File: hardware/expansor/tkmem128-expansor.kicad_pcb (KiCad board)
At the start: 2 copper layers, 78.7 x 45 mm, 4 parts, among them J1 Barramento TK, J2 Passagem, J3 Para a placa principal

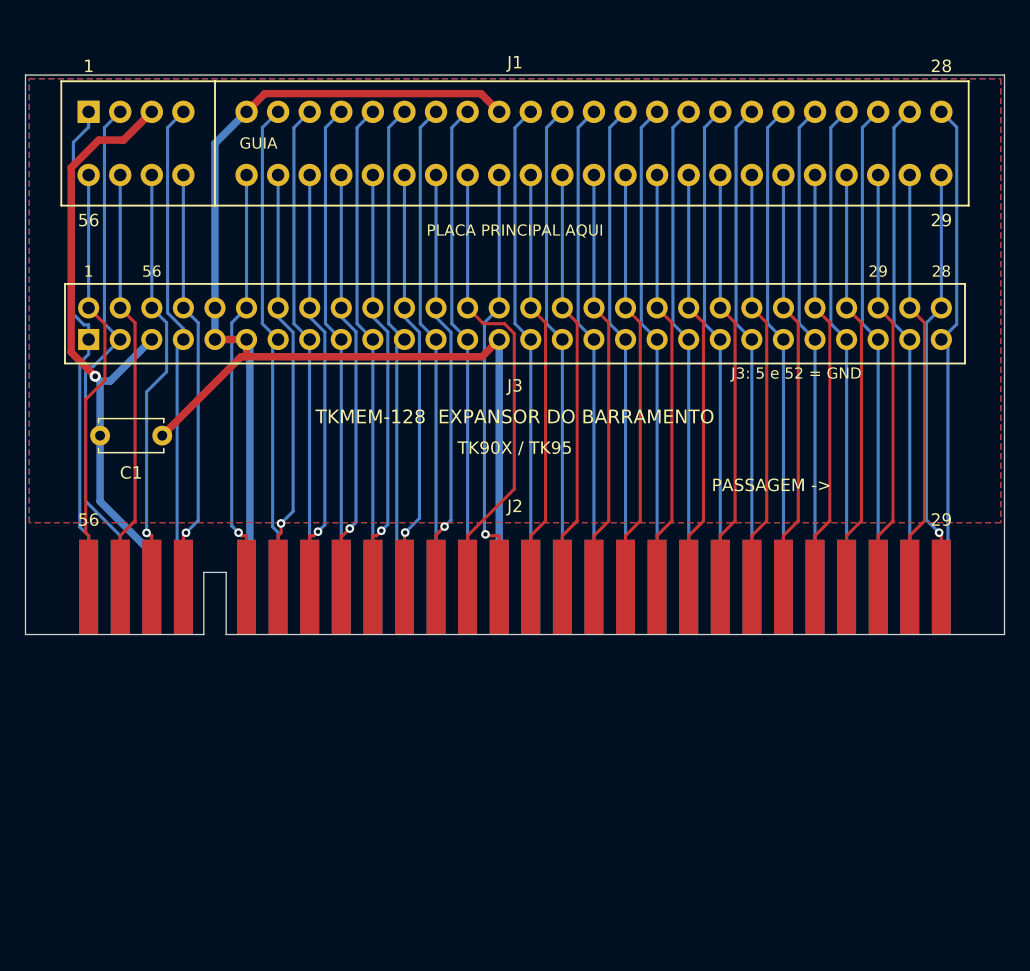
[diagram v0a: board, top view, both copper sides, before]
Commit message: Correcoes de revisao: pino 17, expansora dimensionada, .jed verificado
Correcoes apontadas na revisao:

- "Edu Luccas" -> "Eduardo Luccas" em toda a documentacao.

- O pino 17 do barramento NAO e livre no ZX Spectrum: os pinos 16, 17 e 18
  la sao Y, V e U do video componente. Corrigido na definicao do barramento
  e na documentacao, com aviso explicito de nunca fechar JP4 em Spectrum.
  Isso tambem sustenta a analise de por que a placa original avisava que o
  jumper na posicao errada danificava o micro: o pino util no TK e sinal de
  video no Spectrum, entao o jumper escolhia entre dois pinos diferentes, e
  os dois barramentos divergem justamente em pinos de alimentacao (34, 35,
  37).

- SJ1 e SJ2 sao opcionais e podem ficar abertos em qualquer maquina. O terra
  ja chega pelos pinos 6 e 14, que sao GND nas duas. Deixado explicito no
  README, na montagem e no verso da placa.

- Encaixe na caixa conferido contra os desenhos tecnicos da Patola: a tampa
  tem 81 x 69 mm internos e a placa principal (78,74 x 66,04) cabe com folga.
  Ja a expansora de 45 mm sobrava so 6,5 mm de cada lado da caixa de 32 mm -
  insuficiente para o soquete alcancar o TK. Alongada para 70 mm (19 mm de
  cada lado) e com as paredes da caixa marcadas na serigrafia.

- O .jed do GAL agora vai pronto: hardware/gal/tkmem128.jed, checksum C5752.
  Gerado por tools/galgen.py a partir das equacoes do projeto, com o mapa de
  colunas da matriz AND deduzido das proprias equacoes, e conferido fusivel a
  fusivel contra o mapa de referencia: zero divergencias em 2706 fusiveis.

Roteamento: as duas placas fecham 100% em 2 camadas com isolacao de 0,14 mm.
A ultima ligacao da placa principal exigiu um roteador de labirinto proprio
(tools/maze.py). ERC e DRC zerados; netlist reconferida no a no.

Co-Authored-By: Claude Opus 5 <noreply@anthropic.com>
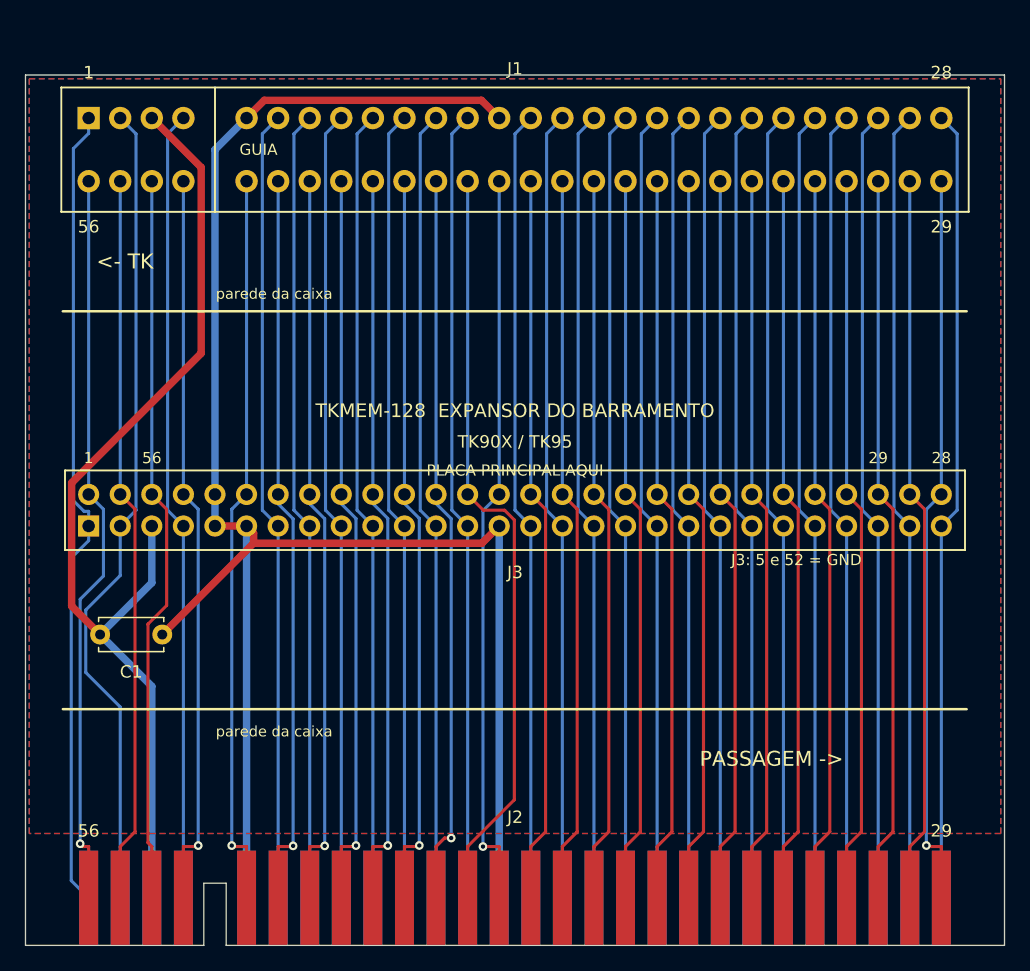
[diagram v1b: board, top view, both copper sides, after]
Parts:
- moved J2 25.0 mm to (39.4, 66.2)
- moved C1 16.0 mm to (6.00, 45.0)
- moved J3 15.0 mm to (39.4, 35.0)
- moved J1 0.50 mm to (39.4, 6.00)
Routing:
- net GND: track 115.2 -> 150.1 mm
- net +5V: track 50.3 -> 81.8 mm, vias 1 -> 0
- net D1: track 34.1 -> 59.2 mm
- net A14: track 40.1 -> 65.1 mm
- net BUS_P29: track 34.1 -> 59.2 mm
- net A15: track 34.4 -> 59.5 mm, vias 0 -> 1
- net BUS_SOUNDIN: track 34.1 -> 59.2 mm
- net D3: track 34.1 -> 59.2 mm
- net D6: track 34.2 -> 59.2 mm
- net D2: track 34.4 -> 59.2 mm
- net D5: track 34.3 -> 59.2 mm
- net D4: track 34.1 -> 59.0 mm
- net D0: track 34.4 -> 59.2 mm
- net BUS_NMI: track 34.7 -> 59.5 mm
- net A10: track 34.1 -> 58.6 mm
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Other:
- board size 78.7 x 45 mm -> 78.7 x 70 mm
- board text added: "<- TK"
- board text added: "parede da caixa"

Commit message: Esquematicos e silk rearranjados; pendencia do plano do soquete de borda
Esquematico das duas placas redesenhado a mao (havia simbolos saindo da
folha e sinais misturados) e serigrafia reorganizada. Conferido: ERC 0,
DRC 0, e a netlist exportada bate no a no com a intencao de projeto nas
duas placas (74 e 53 nets, zero divergencia).

Os geradores em tools/ passam a ser ferramenta de bootstrap: gen_schematic.py
e gen_pcb.py sobrescreveriam o ajuste manual. A fonte corrente e o conteudo
de hardware/. Documentado no README de tools/.

Registrada uma pendencia real da placa expansora (item 1b de
docs/ANTES-DE-FABRICAR.md): nas placas originais a fenda do soquete que
recebe os dedos do TK fica NO PLANO da placa, alinhada com os dedos de
passagem. O footprint atual e uma grade 2x28 de furos comuns, ou seja, o
conector monta por cima e a fenda fica alguns milimetros acima do plano —
o que joga a expansora abaixo do plano do TK e faz o periferico seguinte da
corrente descer outro tanto. Falta medir o conector para decidir entre
straddle mount e montagem por baixo.

Saidas de fabricacao e renders regerados a partir dos arquivos revisados.

Co-Authored-By: Claude Opus 5 <noreply@anthropic.com>
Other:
- board text added: "Derivado de Velesoft 2009 e Luccas Eletrônica 2012"
- board text removed: "Derivado de Velesoft 2009 e Luccas Eletronica 2012"
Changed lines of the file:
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@@
 			(layer "F.CrtYd")
 		)
-		(fp_text user "1"
-			(at -34.29 -4.2 0)
+		(fp_text user "56"
+			(at -37.37 -2 0)
 			(layer "F.SilkS")
 			(effects
@@
 			)
 		)
-		(fp_text user "56"
-			(at -29.21 -4.2 0)
+		(fp_text user "1"
+			(at -37.37 1.5 0)
 			(layer "F.SilkS")
 			(effects
@@
 		)
 		(fp_text user "29"
-			(at 29.21 -4.2 0)
+			(at 37.63 -2 0)
 			(layer "F.SilkS")
 			(effects
@@
 		)
 		(fp_text user "28"
-			(at 34.29 -4.2 0)
+			(at 37.63 2 0)
 			(layer "F.SilkS")
 			(effects
@@
 			(layer "F.CrtYd")
 		)
-		(fp_text user "1"
-			(at -34.29 -6.2 0)
+		(fp_text user "56"
+			(at -37.87 3.5 0)
 			(layer "F.SilkS")
 			(effects
@@
 			)
 		)
-		(fp_text user "56"
-			(at -34.29 6.2 0)
+		(fp_text user "1"
+			(at -37.37 -3 0)
 			(layer "F.SilkS")
 			(effects
@@
 		)
 		(fp_text user "28"
-			(at 34.29 -6.2 0)
+			(at 37.93 -3 0)
 			(layer "F.SilkS")
 			(effects
@@
 		)
 		(fp_text user "29"
-			(at 34.29 6.2 0)
+			(at 37.93 3.5 0)
 			(layer "F.SilkS")
 			(effects
@@
 	)
 	(gr_text "parede da caixa"
-		(at 20 17.6 0)
+		(at 20 20.5 0)
 		(layer "F.SilkS")
 		(effects
@@
 	)
 	(gr_text "parede da caixa"
-		(at 20 52.8 0)
+		(at 20 49.5 0)
 		(layer "F.SilkS")
 		(effects
@@
 		)
 	)
-	(gr_text "PLACA PRINCIPAL AQUI"
-		(at 39.37 31.8 0)
+	(gr_text "J3: 5 e 52 = GND"
+		(at 18.5 39.5 0)
 		(layer "F.SilkS")
 		(effects
@@
 		)
 	)
-	(gr_text "J3: 5 e 52 = GND"
-		(at 62 39 0)
+	(gr_text "PLACA PRINCIPAL AQUI"
+		(at 39 30.8 0)
 		(layer "F.SilkS")
 		(effects
@@
 	)
 	(gr_text "TK90X / TK95"
-		(at 39.37 29.5 0)
+		(at 39 28.5 0)
 		(layer "F.SilkS")
 		(effects
@@
 	)
 	(gr_text "TKMEM-128  EXPANSOR DO BARRAMENTO"
-		(at 39.37 27 0)
+		(at 39 26 0)
 		(layer "F.SilkS")
 		(effects
@@
 		)
 	)
-	(gr_text "<- TK"
-		(at 8 15 0)
+	(gr_text "PASSAGEM ->"
+		(at 71 48 -90)
 		(layer "F.SilkS")
 		(effects
@@
 		)
 	)
-	(gr_text "PASSAGEM ->"
-		(at 60 55 0)
+	(gr_text "<- TK"
+		(at 6.5 24 270)
 		(layer "F.SilkS")
 		(effects
@@
 		)
 	)
-	(gr_text "Derivado de Velesoft 2009 e Luccas Eletronica 2012"
+	(gr_text "Derivado de Velesoft 2009 e Luccas Eletrônica 2012"
 		(at 39.37 47 0)
 		(layer "B.SilkS")

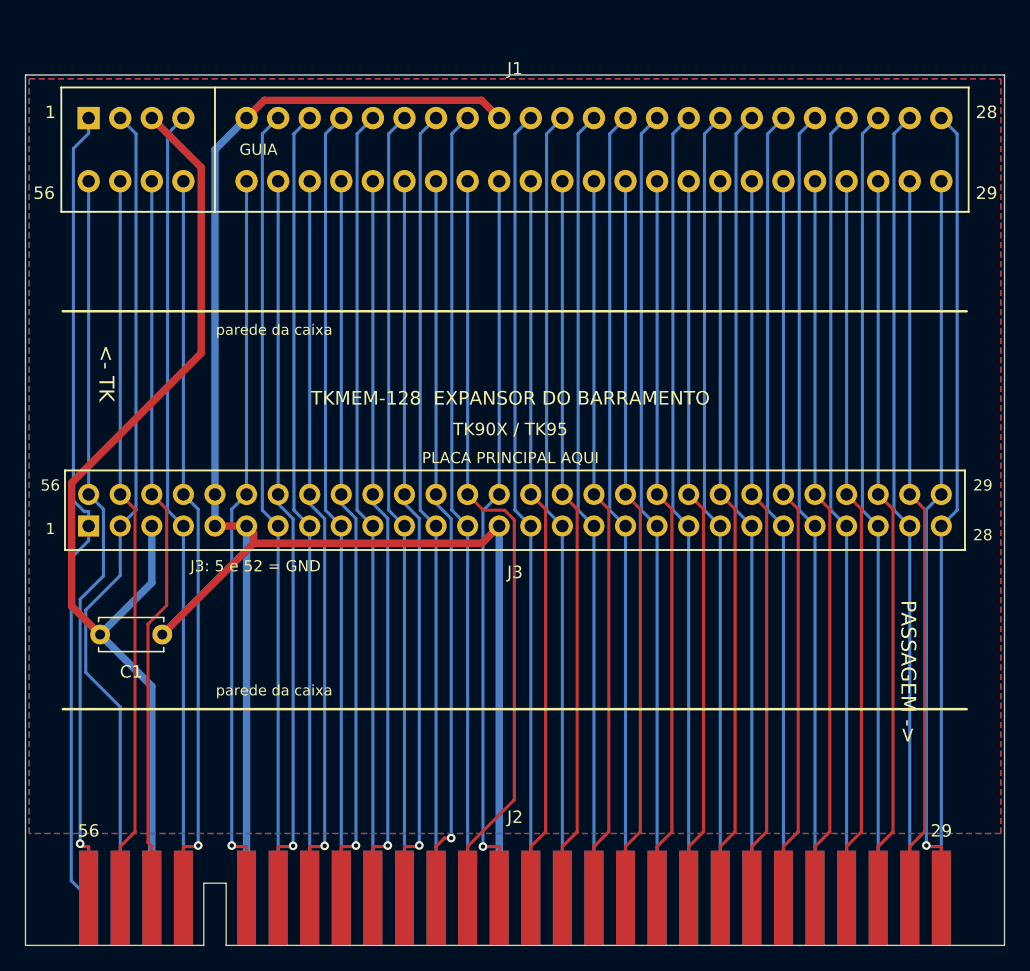
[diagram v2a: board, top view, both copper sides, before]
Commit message: Arquitetura corrigida: conector na placa principal, tira soldada nos terminais
As fotos do periferico de audio (mesma construcao da TKMEM) mostraram como o
conjunto realmente se monta, e o datasheet do TE 5645235 confirmou o porque:

  - o conector de borda e de ENTRADA VERTICAL, ou seja, o cartao entra
    perpendicular a placa que o segura. Por isso ele vai soldado direto na
    placa PRINCIPAL, que fica em pe: a fenda cai no plano horizontal e recebe
    o cartao do TK;
  - os terminais atravessam a placa principal e sobram 3,18 mm do outro lado;
  - a tira de expansao encosta nesses terminais e e soldada neles. Ela nao tem
    conector nenhum: 56 ilhas de solda de um lado, dedos de borda do outro.

Com isso a tira fica coplanar com o cartao do TK e com a fenda do conector, e
a corrente de perifericos nao ganha degrau nenhum - que era o ponto levantado
na revisao.

Mudancas:

  placa principal  J1 troca do header 2x28 para o footprint do conector de
                   borda (2,54 x 4,85 mm, furo 1,02). O esquematico NAO mudou
                   (mesmo simbolo, mesmas nets), entao o rearranjo manual foi
                   preservado; so o cobre foi refeito.
  tira de expansao redesenhada: J1 = ilhas de solda 2x28, J2 = dedos de borda,
                   C1 de desacoplamento. 45 mm de comprimento.
  footprints       soquete passa a ter as 56 posicoes (a guia 5/52 e um
                   pedacinho de PCB que o montador encaixa, o conector tem
                   contato em todas). Novo ZX_TK_Bus_SolderPads_56.

Documentada tambem a orientacao de montagem: o lado dos componentes da placa
principal fica virado para a tira de expansao, nunca para o conector - ao
contrario a placa esbarra no micro dentro da caixa.

ERC 0, DRC 0 e netlist conferida no a no nas duas placas (74 e 53 nets).

Co-Authored-By: Claude Opus 5 <noreply@anthropic.com>
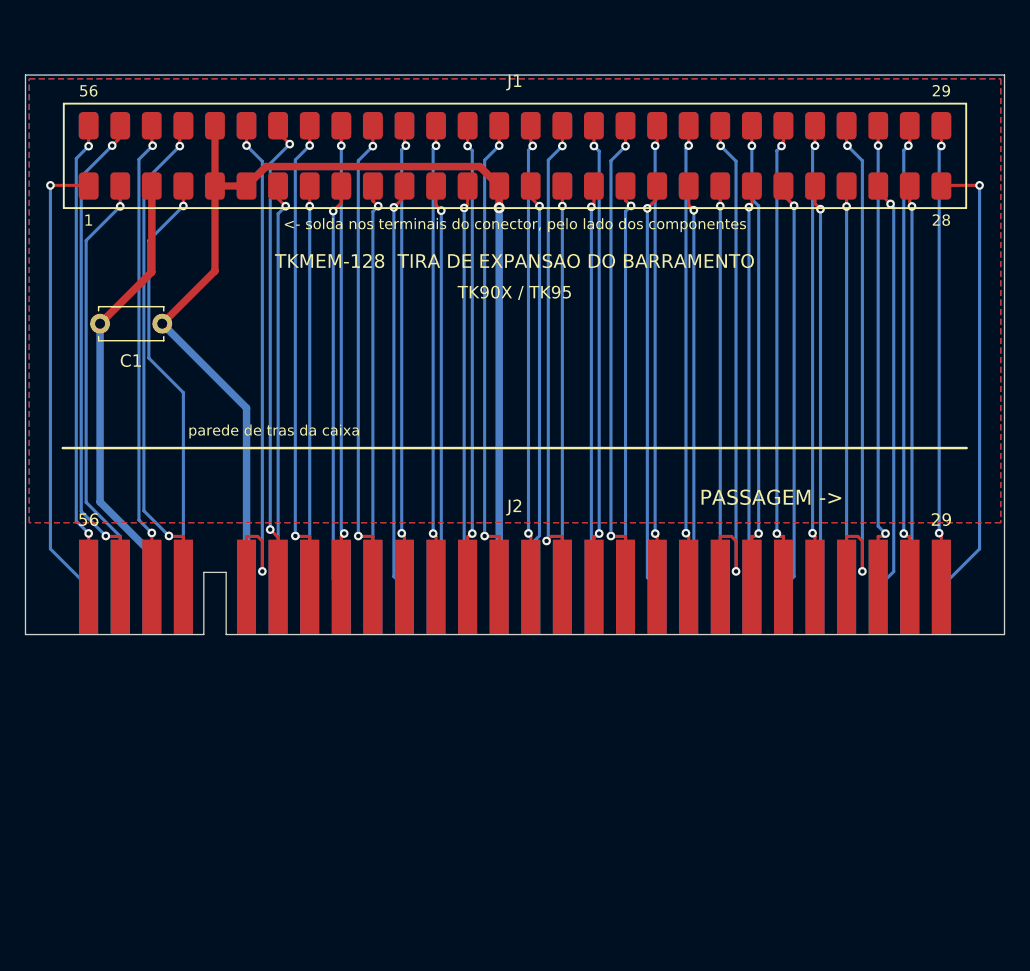
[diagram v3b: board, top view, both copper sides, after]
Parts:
- removed J3: Para a placa principal, ZX_TK_Bus_Header_2x28
- J1: value Barramento TK -> Terminais do conector; footprint ZX_TK_Bus_Socket_56 -> ZX_TK_Bus_SolderPads_56
- moved C1 25.0 mm to (6.00, 20.0)
- moved J2 25.0 mm to (39.4, 41.2)
- moved J1 0.50 mm to (39.4, 6.50)
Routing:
- net GND: track 150.1 -> 98.1 mm, vias 0 -> 1
- net +5V: track 81.8 -> 35.7 mm
- net A12: track 66.1 -> 34.5 mm, vias 0 -> 1
- net ROMCS_BUS: track 63.8 -> 32.3 mm, vias 0 -> 1
- net A7: track 63.8 -> 32.3 mm, vias 0 -> 1
- net BUS_P16: track 63.8 -> 32.3 mm, vias 0 -> 1
- net BUS_CLK: track 63.8 -> 32.3 mm, vias 0 -> 1
- net A9: track 63.8 -> 32.4 mm, vias 0 -> 1
- net RAMDIS: track 63.8 -> 32.4 mm, vias 0 -> 1
- net A6: track 63.8 -> 32.5 mm, vias 0 -> 1
- net BUS_IORQGE: track 63.8 -> 32.5 mm, vias 0 -> 1
- net RESET_N: track 63.8 -> 32.6 mm, vias 0 -> 1
- net A3: track 63.8 -> 32.6 mm, vias 0 -> 1
- net A1: track 63.8 -> 32.6 mm, vias 0 -> 1
- net A4: track 63.8 -> 32.6 mm, vias 0 -> 1
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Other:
- board size 78.7 x 70 mm -> 78.7 x 45 mm
- board text added: "<- solda nos terminais do conector, pelo lado dos componentes"
- board text added: "Derivado de Velesoft 2009 e Luccas Eletronica 2012"
- board text added: "TKMEM-128 TIRA DE EXPANSAO DO BARRAMENTO"
- board text added: "parede de tras da caixa"
- board text removed: "<- TK"
- board text removed: "Derivado de Velesoft 2009 e Luccas Eletrônica 2012"
- board text removed: "J3: 5 e 52 = GND"
- board text removed: "PLACA PRINCIPAL AQUI"
- board text removed: "TKMEM-128 EXPANSOR DO BARRAMENTO"
- board text removed: "parede da caixa"

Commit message: Conector no verso, sem furos na guia, tira soldada dos dois lados
Tres correcoes de revisao:

1. A guia ocupa a posicao das vias 5 e 52, entao nao ha terminal ali e a placa
   nao precisa de furo. Footprint do conector volta de 56 para 54 furos. O
   simbolo continua com 56 pinos, o que deixou o esquematico rearranjado a mao
   intacto - o KiCad aceita os dois pinos sem ilha e o DRC fica zerado (sao
   GND, que tem ilha de sobra).

2. A placa principal estava invertida em relacao ao conector. Ele e o UNICO
   componente do lado do cobre: entra por baixo e e soldado por cima, pelo lado
   dos componentes, que fica virado para a tira de expansao. J1 passa para a
   camada B.Cu. O espelhamento que vem junto e a consequencia fisica de enfiar
   a peca pelo outro lado, e reforca o teste de continuidade do item 2.

3. A tira nao encosta nos terminais por fora: os terminais sao RETOS e ficam em
   duas fileiras a 4,85 mm, entao a tira entra ENTRE elas - uma fileira por
   cima, outra por baixo - e e soldada dos DOIS LADOS. O footprint passa a ter
   ilhas nas duas faces (F.Cu = 29..56, B.Cu = 1..28), nao SMD de uma face so.

Roteamento refeito nas duas placas, ambas 100% fechadas em 2 camadas com
isolacao de 0,14 mm. ERC 0, DRC 0 erros, 0 desconexoes, netlist conferida no a
no (74 e 53 nets). A serigrafia ajustada a mao foi preservada.

Co-Authored-By: Claude Opus 5 <noreply@anthropic.com>
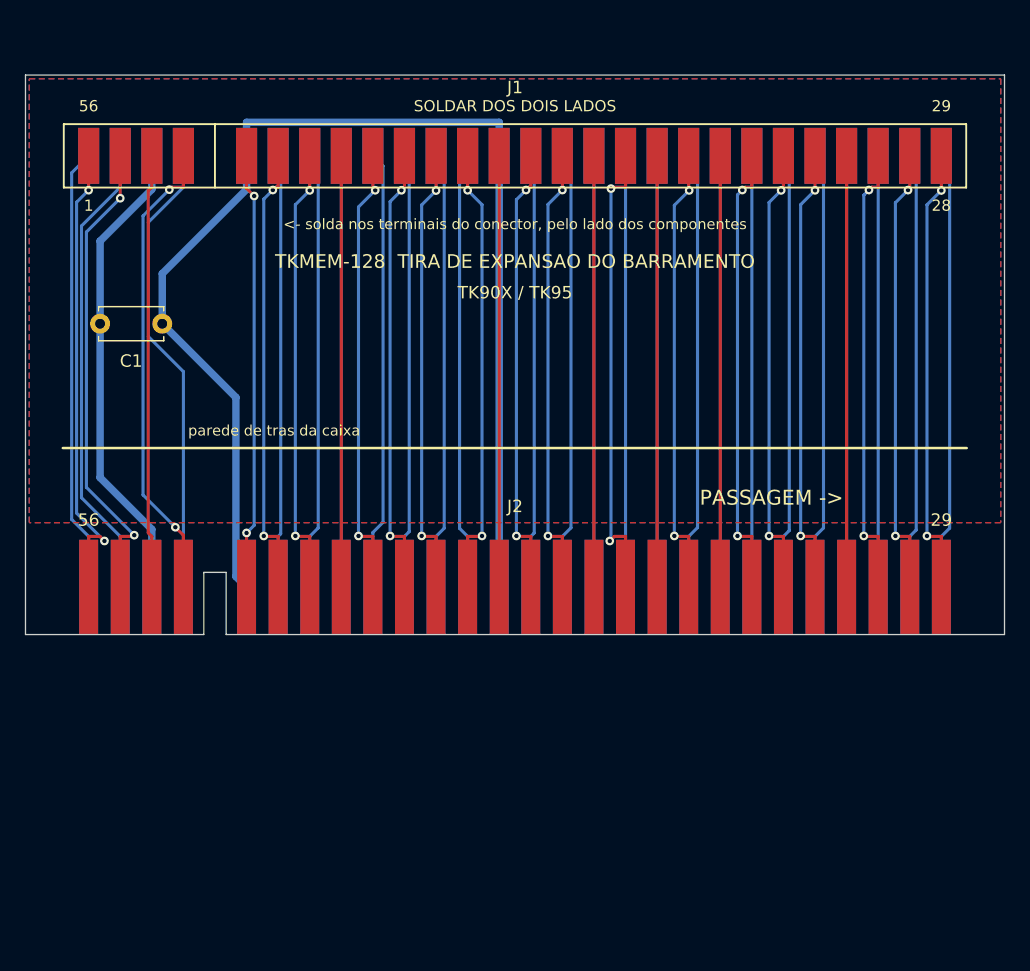
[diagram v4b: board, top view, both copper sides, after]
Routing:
- net BUS_WAIT: track 44.3 -> 34.7 mm, vias 2 -> 0
- net BUS_RFSH: track 44.2 -> 34.7 mm, vias 2 -> 0
- net D0: track 44.3 -> 35.2 mm
- net BUS_NMI: track 38.7 -> 34.7 mm, vias 2 -> 0
- net MREQ_N: track 39.4 -> 36.2 mm
- net D7: track 37.9 -> 34.9 mm, vias 2 -> 0
- net BUS_P16: track 32.3 -> 35.3 mm, vias 1 -> 0
- net BUS_CLK: track 32.3 -> 35.3 mm, vias 1 -> 0
- net IORQ_N: track 37.6 -> 34.7 mm, vias 2 -> 0
- net A1: track 32.6 -> 35.4 mm, vias 1 -> 0
- net A12: track 34.5 -> 37.3 mm, vias 1 -> 0
- net BUS_IORQGE: track 32.5 -> 35.2 mm, vias 1 -> 0
- net A9: track 32.4 -> 35.1 mm, vias 1 -> 0
- net RESET_N: track 32.6 -> 35.3 mm, vias 1 -> 0
- net A4: track 32.6 -> 35.3 mm, vias 1 -> 0
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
